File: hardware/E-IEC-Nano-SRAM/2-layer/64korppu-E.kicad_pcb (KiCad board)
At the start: 2 copper layers, 90 x 70 mm, 41 parts, among them J1 DIN-6_IEC, J2 Floppy_34pin, J3 DC_Jack, U1 Arduino_Nano, U2 23LC256, U3 74HC595

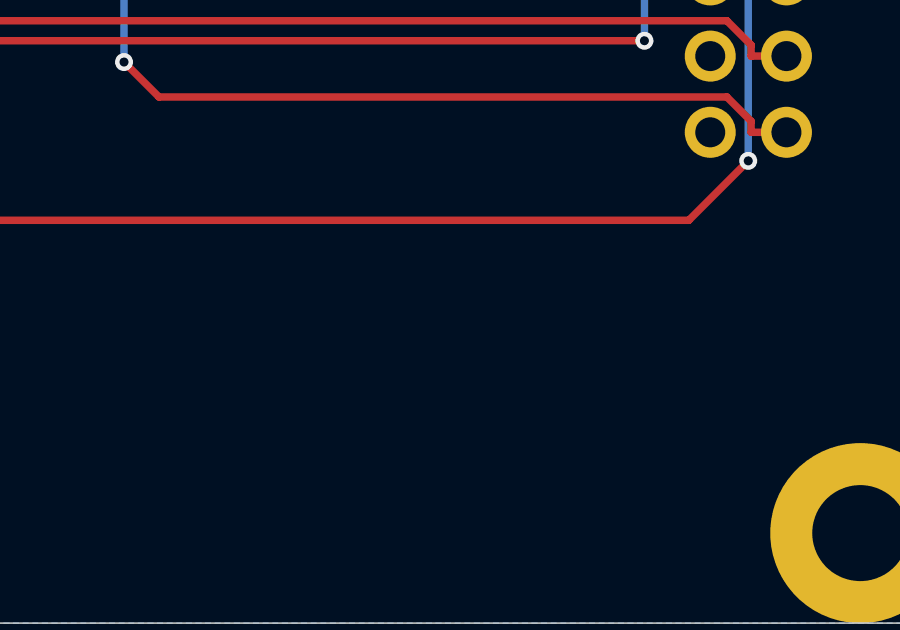
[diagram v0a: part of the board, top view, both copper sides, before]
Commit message: Add "karski by design 2026 rev 001" board label to both PCBs
Add copper layer text label on F.Cu for 2-layer and 4-layer PCBs.
Resize script recreates the label automatically on each resize.
Fix SetIsBold→SetBold for KiCad 9 Python API.

Co-Authored-By: Claude Opus 4.6 <noreply@anthropic.com>
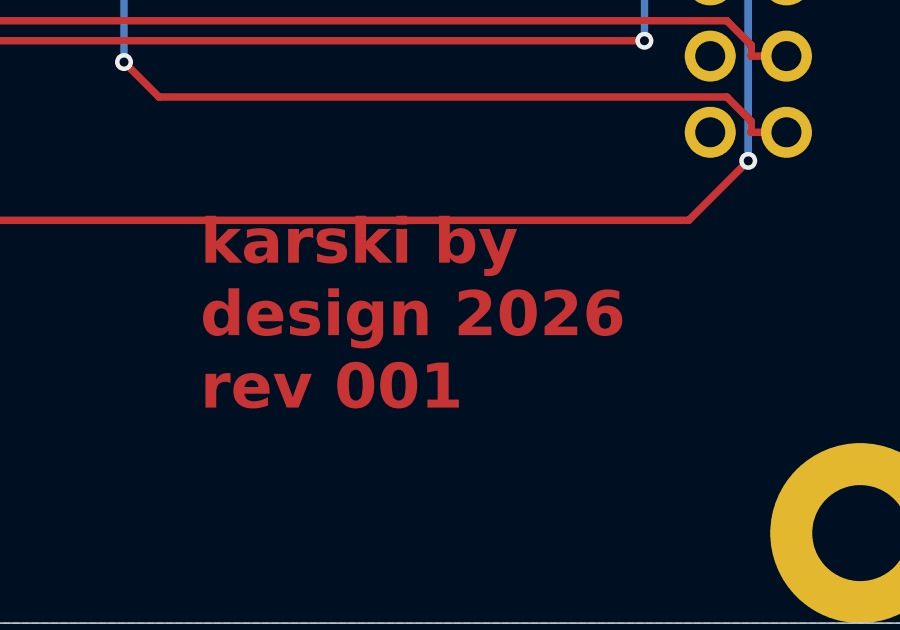
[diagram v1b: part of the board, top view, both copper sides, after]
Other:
- board text added: "karski by design 2026 rev 001"
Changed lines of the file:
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@@
 		(layer "Edge.Cuts")
+	)
+	(gr_text "karski by\ndesign 2026\nrev 001"
+		(at 165 163 0)
+		(layer "F.Cu")
+		(effects
+			(font
+				(size 1.5 1.5)
+				(thickness 0.3)
+				(bold yes)
+			)
+			(justify left bottom)
+		)
 	)
 	(segment
